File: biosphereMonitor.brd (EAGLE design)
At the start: 85 x 85 mm, 49 parts, among them IC1 XMEGA32A4AU, IC2 LM35, IC3 FT232RL, IC4 NE555D, Q1 16Mhz, Q2 32kHz

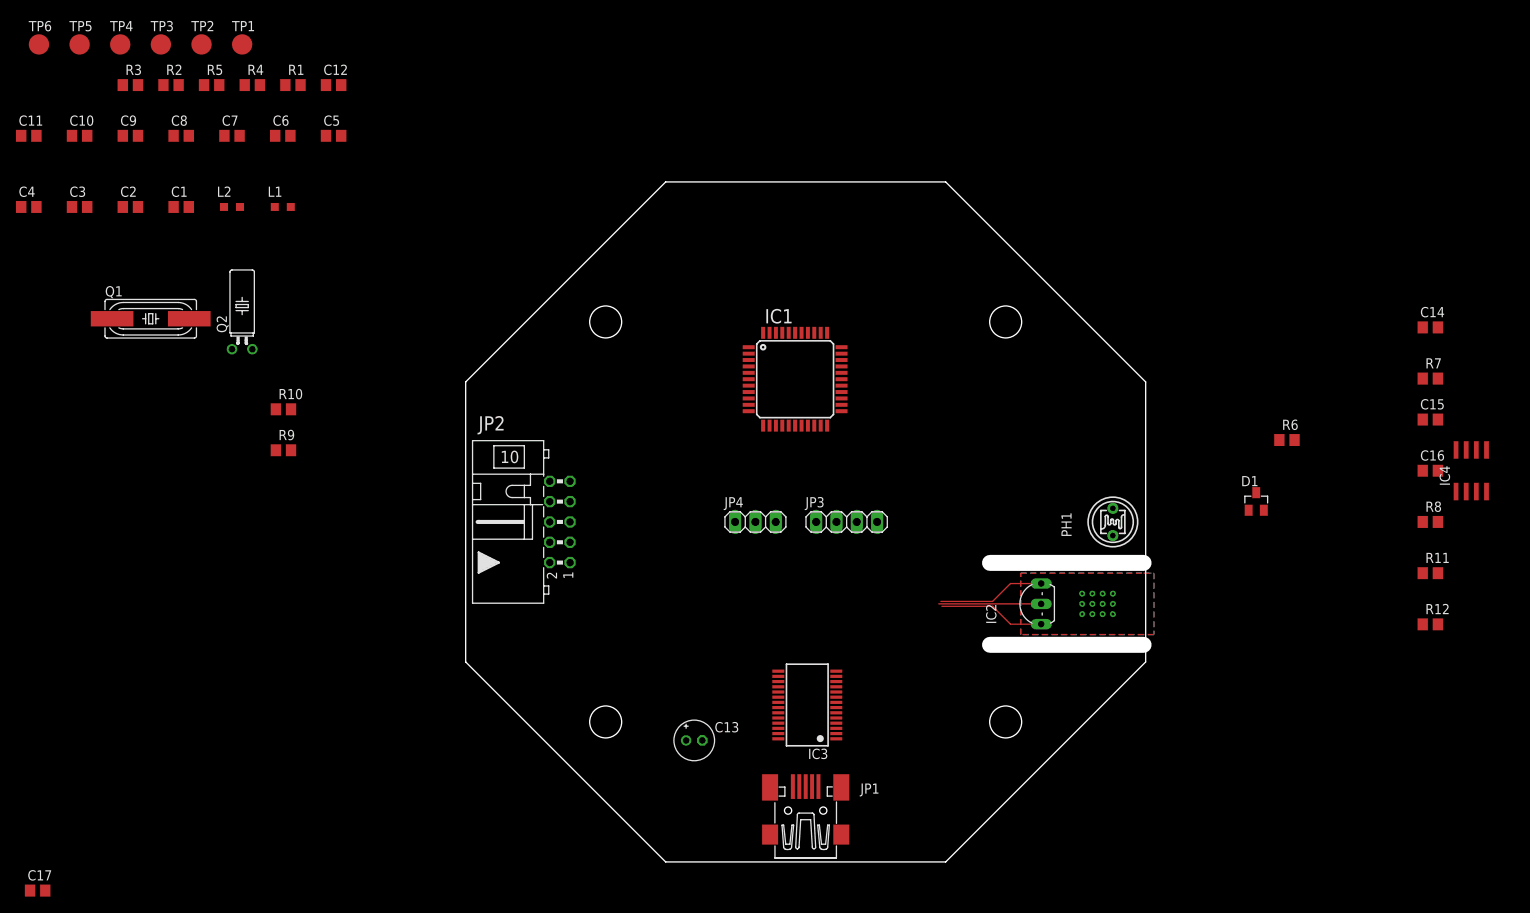
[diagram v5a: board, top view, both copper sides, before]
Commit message: added humidity conversion to percent and completed schematic
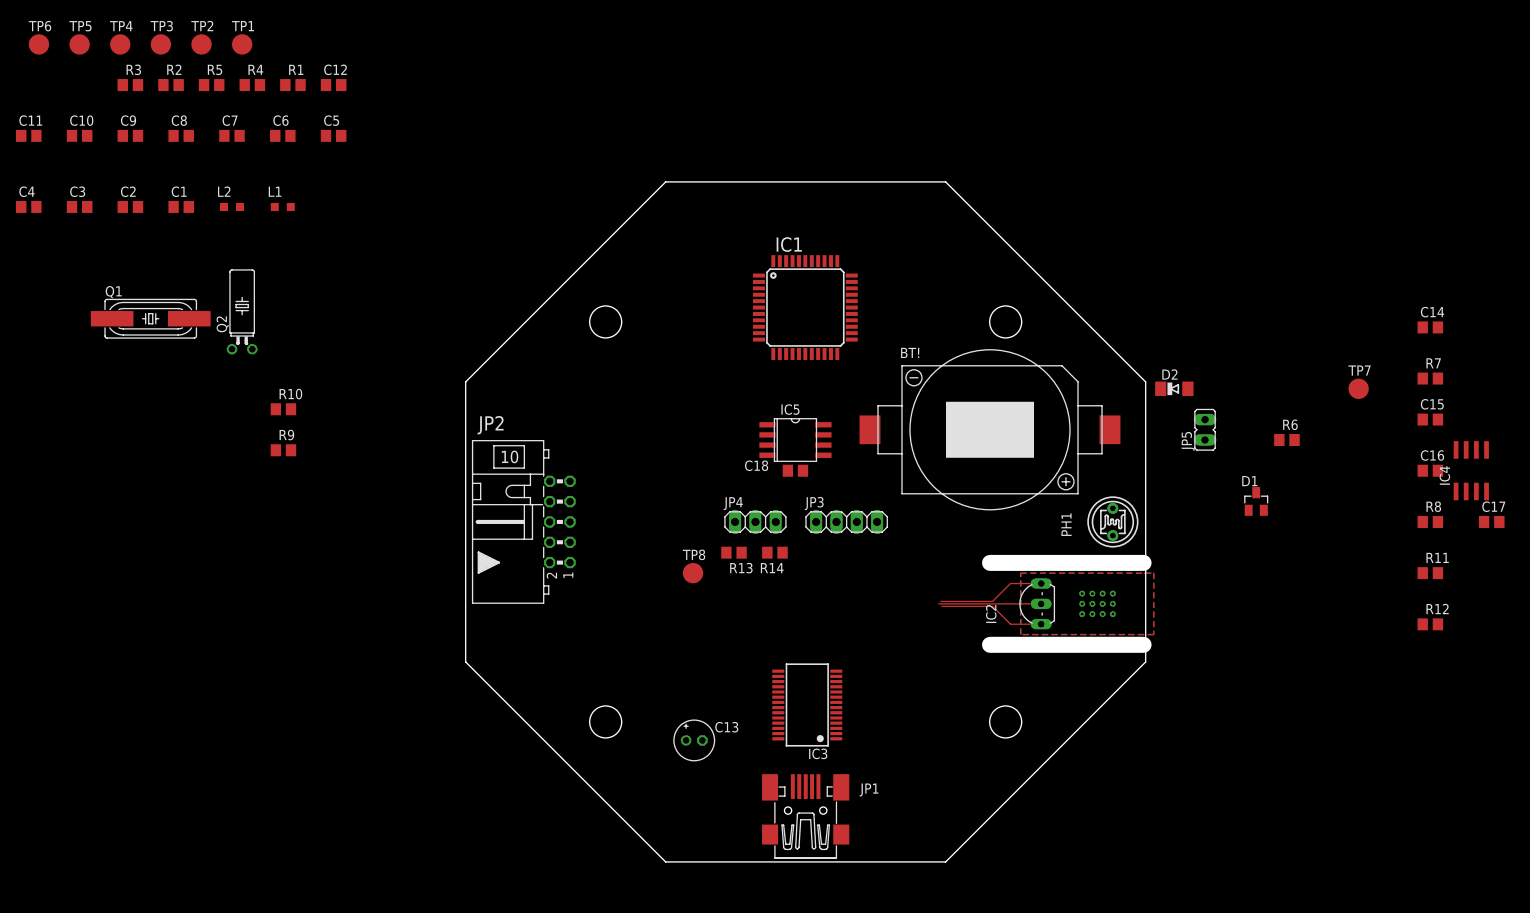
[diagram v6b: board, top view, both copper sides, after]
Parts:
- added BT!: CR2032, Tjarks_Bauteile (1):CR2032
- added C18: 100n, rcl:C0805
- added D2: 1N4148, diode:MINIMELF
- added IC5: SST25VF040, Tjarks_Bauteile (1):SO08-208
- added JP5: (no value), jumper:JP1
- added R13: 22k, rcl:R0805
- added R14: 10k, rcl:R0805
- added TP7, TP8: PTR1B2,54, testpad:B2,54
- R10: value 3k3 -> 33k
- R9: value 2k2 -> 22k
- moved C17 187.5 mm to (85.8, 0.00)
- moved IC1 9.05 mm to (-0.04, 26.8)
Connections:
- new net MEM_CE: IC1.14, IC5.1
- new net MEM_HOLD: IC1.20, IC5.7
- new net MEM_MISO: IC1.16, IC5.2
- new net MEM_MOSI: IC1.15, IC5.5
- new net MEM_SCK: IC1.17, IC5.6
- new net MEM_WP: IC1.21, IC5.3
- new net N$25: JP4.1, R13.1
- new net N$26: BT!.+, JP5.1
- new net N$27: D2.A, JP5.2
- net +3V3: now also C18.2, D2.C, IC5.8
- net GND: now also BT!.-, C18.1, IC5.4, R14.2
- net LIGHT: now also TP7.TP
- net SOIL: now also R13.2, R14.1, TP8.TP; no longer JP4.1

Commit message: placed Parts
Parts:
- removed BT!: CR2032, Tjarks_Bauteile (1):CR2032
- added BT1: CR2032, Tjarks_Bauteile (1):CR2032
- added C19: 4,7µF, rcl:E2-5
- added R15: 10k, rcl:R0805
- D1: value LM4050 2.5 -> 2.5
- JP5: value (none) -> BAT
- PH1: value BPW 96C TEL -> BPW 96
- moved TP6 133.1 mm to (15.5, -13.3)
- moved R3 128.4 mm to (11.5, -30.7)
- moved R2 122.9 mm to (11.5, -28.2)
- moved C10 121.5 mm to (7.68, -23.0), turned to 270 degrees
- moved TP5 118.2 mm to (-15.2, -31.2)
- moved TP3 114.2 mm to (-11.5, -31.2)
- moved TP4 112.6 mm to (-19.1, -31.2)
- moved C11 112.5 mm to (2.56, -3.84), turned to 180 degrees
- moved C17 111.3 mm to (-24.3, 16.6), turned to 90 degrees
- moved C4 106.7 mm to (8.96, 28.2), turned to 90 degrees
- moved R8 106.3 mm to (-26.9, 16.6), turned to 90 degrees
- moved R5 102.4 mm to (8.96, -5.12), turned to 270 degrees
- moved R12 102.2 mm to (-16.6, 25.6), turned to 180 degrees
- moved IC4 101.6 mm to (-17.9, 16.6), turned to 180 degrees
- moved C6 101.0 mm to (18.8, -7.60), turned to 270 degrees
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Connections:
- net D+ renamed D_P
- net D- renamed D_N
- net N$9 renamed AVCC
- net USB_MC_D+ renamed USB_MC_D_P
- net USB_MC_D- renamed USB_MC_D_N
- new net N$28: IC3.19, R15.2
- net +3V3: now also C19.+, R15.1
- net GND: now also BT1.-, C19.-; no longer BT!.-
- net N$26: now also BT1.+; no longer BT!.+
- net N$5: now also Q2.1; no longer Q2.2
- net N$6: now also Q2.2; no longer Q2.1
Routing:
- net USB_MC_D_P: track 0.00 -> 60.2 mm
- net USB_MC_D_N: track 0.00 -> 58.0 mm
- net D_N: track 0.00 -> 21.2 mm
- net D_P: track 0.00 -> 20.8 mm

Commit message: routed board
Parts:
- moved C2 15.4 mm to (16.6, 37.1)
- moved TP8 13.1 mm to (-1.28, -8.96)
- moved TP3 3.84 mm to (-15.3, -31.2)
- moved TP5 3.84 mm to (-11.4, -31.2)
- moved Q1 2.56 mm to (7.63, 37.3)
- moved R10 2.56 mm to (-14.1, 35.8)
- moved R9 2.56 mm to (-14.1, 38.4)
- moved C7 1.28 mm to (1.25, 17.5)
- moved C9 0.90 mm to (-8.06, 25.1)
- moved L2 0.50 mm to (-5.62, 38.4)
- moved C4 0.26 mm to (8.96, 27.9)
- turned C1 to 270 degrees
- turned C13 to 180 degrees
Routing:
- net GND: track 13.5 -> 468.5 mm, vias 0 -> 15
- net +3V3: track 0.00 -> 216.9 mm, vias 0 -> 8
- net +5V: track 13.3 -> 203.0 mm, vias 0 -> 11
- net N$1: track 0.00 -> 88.5 mm, vias 0 -> 2
- net N$2: track 0.00 -> 70.0 mm, vias 0 -> 2
- net T_OUT: track 12.8 -> 74.7 mm, vias 0 -> 2
- net SOIL: track 0.00 -> 58.8 mm, vias 0 -> 2
- net USB_RX: track 0.00 -> 50.3 mm
- net USB_TX: track 0.00 -> 49.0 mm
- net BME_SDA: track 0.00 -> 42.6 mm, vias 0 -> 1
- net BME_SCL: track 0.00 -> 38.8 mm, vias 0 -> 1
- net LIGHT: track 0.00 -> 34.2 mm, vias 0 -> 2
- net MEM_WP: track 0.00 -> 23.9 mm
- net N$21: track 0.00 -> 21.9 mm, vias 0 -> 2
- net 1V: track 0.00 -> 19.2 mm
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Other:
- board text added: "Biosphere Monitor"
- board text added: "Version 1.0 Tjark Gaudich 2021 github.com/TjarkG"
